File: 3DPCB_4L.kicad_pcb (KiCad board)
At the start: 4 copper layers, 100 x 60 mm, 757 parts, among them IC1 DRV8825, IC2 DRV8825, IC3 DRV8825, IC4 DRV8825, IC5 DRV8825, IC6 MP9943, J10 , J11 , J12 , J13 , J14 , J15 , J16 , J2 , J3 , J4 , J5 , J6 , J7 , J8 , J9 , K1 CONN_3, K2 CONN_3, K3 CONN_3, K4 CONN_3, K5 CONN_3, K6 CONN_3, K7 CONN_3, K8 CONN_3, K9 CONN_3, P1 CONN_8, P11 CONN_3X2, P12 CONN_3X2, P13 CONN_4, P2 CONN_8, P5 CONN_4, P6 CONN_4, P7 CONN_4, P8 CONN_2, P9 CONN_4, U1 CONN_4_LERCHE, U10 MICRO-SD, U11 TC4427, U12 MCP4728, U13 CONN_4_LERCHE, U15 SPST_MOMENTARY, U16 CONN_4_LERCHE, U2 SPST_MOMENTARY, U21 CONN_4_LERCHE, U22 CONN_4_LERCHE, U23 MCP4728, U24 IRFH5302, U25 CONN_4_LERCHE, U3 BSS84, U4 CONN_4_LERCHE, U5 IRFH5302, U6 LPC1768_TQFP100, U7 IRFH5302, U8 IRFH5302, U9 TC4427

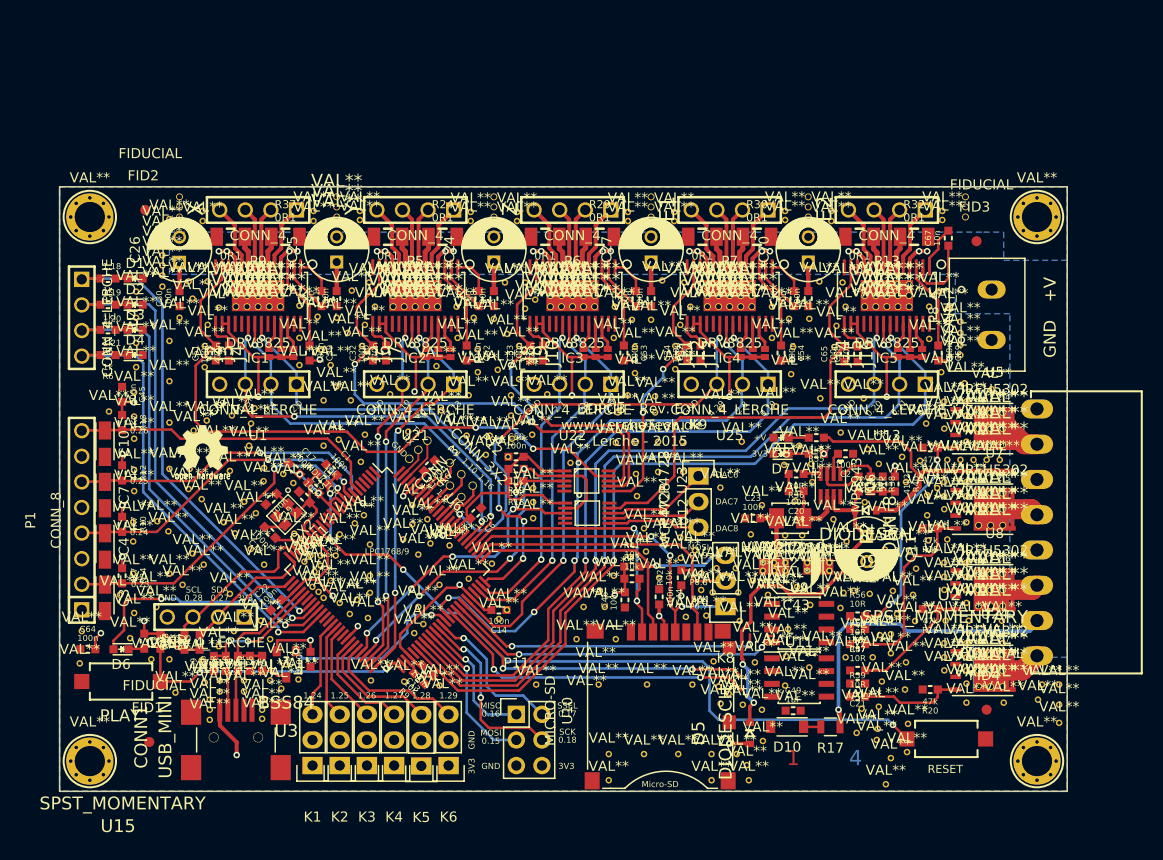
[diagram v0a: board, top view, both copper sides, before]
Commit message: Updated PCB
Updated PCB, splitting power for MOSFETs and motor-drivers.
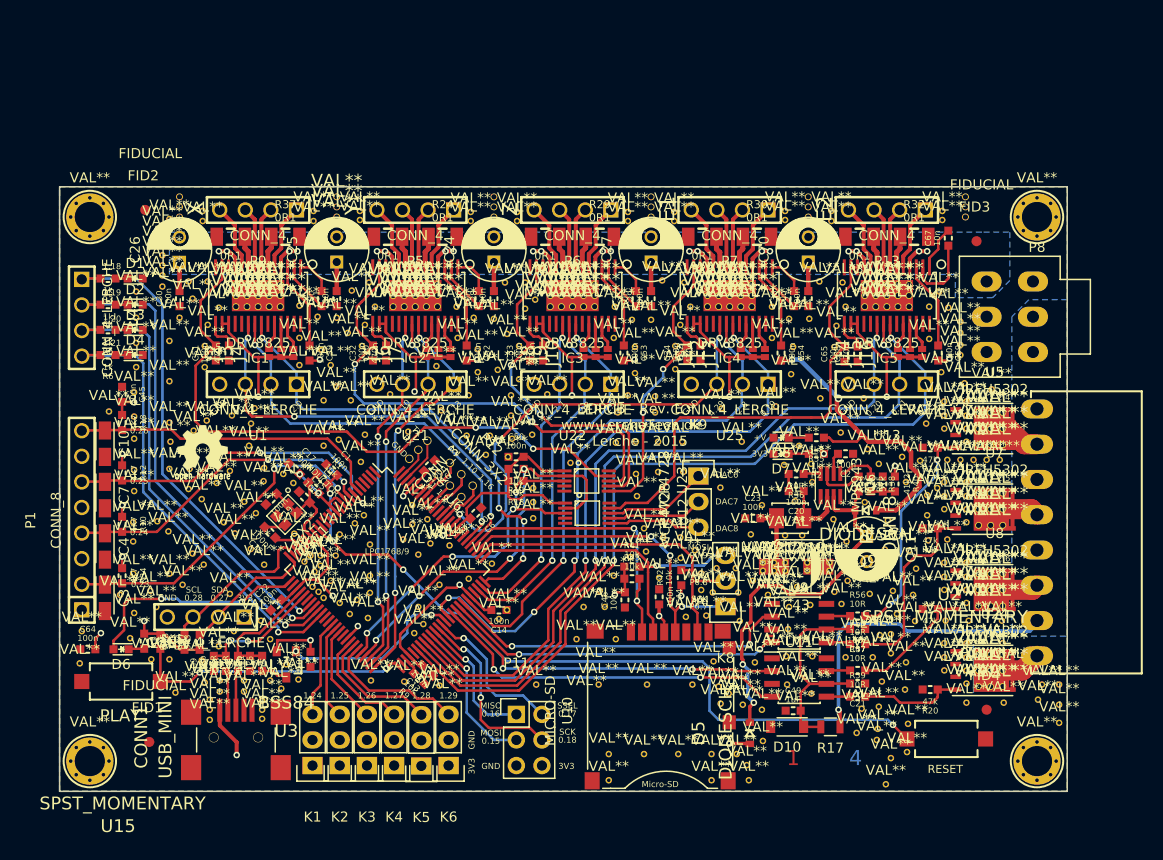
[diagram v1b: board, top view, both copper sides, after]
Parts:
- added ?: VAL**, Lerche_via_0.35_GND, F.Cu at (145.6, 164.9)
- added ?: VAL**, Lerche_via_0.35_GND, F.Cu at (141.0, 160.8)
- added ?: VAL**, Lerche_via_0.35_GND, F.Cu at (202.4, 177.2)
- added ?: VAL**, Lerche_via_0.35_GND, F.Cu at (204.6, 185.8)
- P8: value CONN_2 -> CONN_02X03; footprint LercheTech:Lerche_2P_5MM -> LercheTech:Lerche_2x3P_3.5mm_Molex_UltraFit
- moved P8 1.81 mm to (224.3, 148.4), turned to 270 degrees
- moved ? 1.17 mm to (208.2, 174.6)
- moved ? 1.14 mm to (204.7, 182.1)
- moved ? 0.91 mm to (206.9, 175.7)
- moved ? 0.41 mm to (207.6, 176.9)
- moved ? 0.22 mm to (202.2, 184.9)
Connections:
- CONN1 pad 4: (no net) -> Net-(CONN1-Pad4)
- IC1 pad 18: (no net) -> ~FAULT1
- IC1 pad 19: (no net) -> Net-(IC1-Pad19)
- IC1 pad 27: (no net) -> ~HOME1
- IC2 pad 18: (no net) -> ~FAULT2
- IC2 pad 19: (no net) -> Net-(IC2-Pad19)
- IC2 pad 27: (no net) -> ~HOME2
- IC3 pad 18: (no net) -> ~FAULT3
- IC3 pad 19: (no net) -> Net-(IC3-Pad19)
- IC3 pad 27: (no net) -> ~HOME3
- IC4 pad 18: (no net) -> ~FAULT4
- IC4 pad 19: (no net) -> Net-(IC4-Pad19)
- IC4 pad 27: (no net) -> ~HOME4
- IC5 pad 18: (no net) -> ~FAULT5
- IC5 pad 19: (no net) -> Net-(IC5-Pad19)
- IC5 pad 27: (no net) -> ~HOME5
- IC6 pad 8: (no net) -> Net-(IC6-Pad8)
- P2 pad 2: +12V -> V_MOSFET
- P2 pad 4: +12V -> V_MOSFET
- P2 pad 6: +12V -> V_MOSFET
- P2 pad 8: +12V -> V_MOSFET
- R17 pad 1: +12V -> V_MOSFET
- U10 pad 9: (no net) -> Net-(U10-Pad9)
- U12 pad 5: (no net) -> Net-(U12-Pad5)
- U23 pad 5: (no net) -> Net-(U23-Pad5)
- U6 pad 1: (no net) -> Net-(U6-Pad1)
- U6 pad 100: (no net) -> Net-(U6-Pad100)
- U6 pad 13: (no net) -> Net-(U6-Pad13)
- U6 pad 14: (no net) -> Net-(U6-Pad14)
- U6 pad 16: (no net) -> Net-(U6-Pad16)
- U6 pad 18: (no net) -> Net-(U6-Pad18)
- U6 pad 2: (no net) -> Net-(U6-Pad2)
- U6 pad 20: (no net) -> P1.31
- U6 pad 21: (no net) -> P1.30
- U6 pad 23: (no net) -> Net-(U6-Pad23)
- U6 pad 27: (no net) -> SD_IRQ
- U6 pad 3: (no net) -> Net-(U6-Pad3)
- U6 pad 36: (no net) -> P1.22
- U6 pad 37: (no net) -> P1.23
- U6 pad 4: (no net) -> Net-(U6-Pad4)
- U6 pad 5: (no net) -> Net-(U6-Pad5)
- U6 pad 52: (no net) -> SD_CD
- U6 pad 82: (no net) -> Net-(U6-Pad82)
- U6 pad 86: (no net) -> Net-(U6-Pad86)
- U6 pad 89: (no net) -> Net-(U6-Pad89)
- U6 pad 92: (no net) -> Net-(U6-Pad92)
- U6 pad 95: (no net) -> Net-(U6-Pad95)
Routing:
- net V_MOSFET: track 0.00 -> 30.4 mm, vias 0 -> 1
- net +12V: track 106.9 -> 78.2 mm, vias 27 -> 26
- net MOSVCC: track 2.15 -> 21.3 mm
- net P2.7: track 32.6 -> 35.9 mm
- net P2.4: track 31.3 -> 34.4 mm
- net P2.6: track 31.7 -> 34.5 mm
- net Net-(R56-Pad1): track 0.09 -> 2.47 mm
- net Net-(R57-Pad1): track 0.18 -> 2.56 mm
- net Net-(R59-Pad1): track 0.01 -> 2.37 mm
- net Net-(R58-Pad1): track 0.28 -> 2.43 mm
- net P2.5: track 32.2 -> 33.4 mm
- added copper zone on B.Cu, net V_MOSFET
- added copper zone on Inner2.Cu, net V_MOSFET
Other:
- board text added: "VMOS"
- board text added: "VMOT"
- board text removed: "Three Dimensional Printer Controller Board (3DPCB) - Rev. E Smoothie-compatible - www.smoothieware.org"

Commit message: Minor changes DONT USE NOW
Do not use this right now, changes are still coming in.
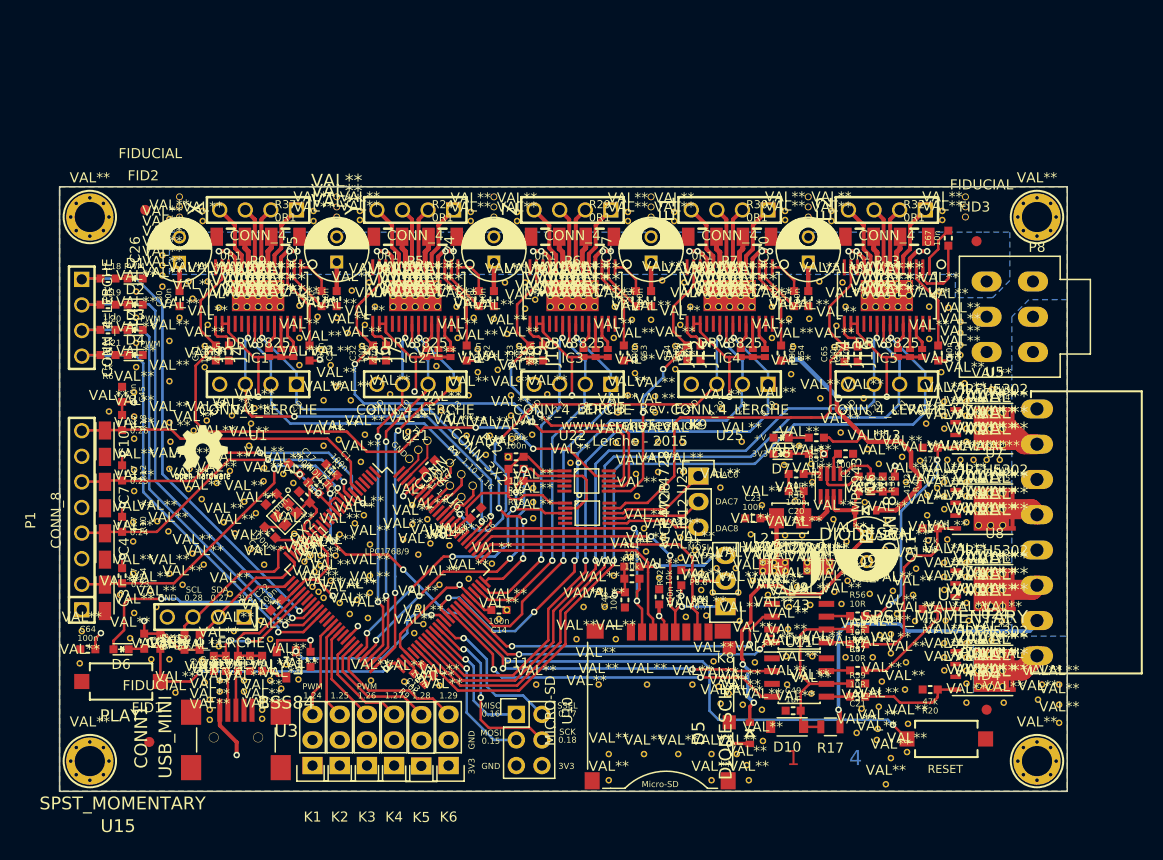
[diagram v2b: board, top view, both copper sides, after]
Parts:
- L2: value IHLP1212-10uH -> IHLP1212-2.2uH
- moved ? 1.14 mm to (222.5, 180.5)
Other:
- board text added: "PWM"
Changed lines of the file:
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@@
 (kicad_pcb (version 4) (host pcbnew 4.0.2-stable)
   (general
-    (links 1061)
+    (links 0)
     (no_connects 0)
-    (area 129.924999 135.424999 230.075001 195.575001)
+    (area 125.893917 130.7236 237.651491 200.3226)
     (thickness 1.6)
-    (drawings 128)
+    (drawings 135)
     (tracks 1506)
     (zones 0)
@@
   )
   (setup
-    (last_trace_width 0.254)
+    (last_trace_width 0.1524)
     (user_trace_width 0.2)
     (user_trace_width 0.254)
@@
     (mod_text_size 1 1)
     (mod_text_width 0.15)
-    (pad_size 1.58 2.35)
-    (pad_drill 0)
+    (pad_size 2 3)
+    (pad_drill 1.2)
     (pad_to_mask_clearance 0)
     (aux_axis_origin 130 195.5)
@@
   )
   (module Lerche_via_0.35mm_GND_MaskOver (layer F.Cu)
-    (at 223.6 180.8)
+    (at 222.5 180.5)
     (attr smd)
     (fp_text reference "" (at 0 -2.9) (layer F.SilkS)
@@
   (module LercheTech:Lerche_IHLP-1212BZ-11_Inductor (layer F.Cu)
     (at 202.5 168.4 180)
-    (fp_text reference L2 (at 0 -4.4 180) (layer F.SilkS)
+    (fp_text reference L2 (at 2.9 -2 180) (layer F.SilkS)
       (effects (font (size 1 1) (thickness 0.15)))
     )
-    (fp_text value IHLP1212-10uH (at 0 -2.9 180) (layer F.SilkS)
+    (fp_text value IHLP1212-2.2uH (at 0 -2.9 180) (layer F.SilkS)
       (effects (font (size 1 1) (thickness 0.15)))
     )
@@
     (fp_line (start -6 5) (end 6 5) (layer F.SilkS) (width 0.15))
     (pad 1 thru_hole oval (at -3.5 -2.3 270) (size 2 3) (drill 1.2) (layers *.Cu *.Mask F.SilkS)
-      (net 19 GND))
+      (net 19 GND) (zone_connect 2))
     (pad 2 thru_hole oval (at -3.5 2.3 270) (size 2 3) (drill 1.2) (layers *.Cu *.Mask F.SilkS)
       (net 1 +12V))
@@
       (net 189 V_MOSFET))
     (pad 4 thru_hole oval (at 0 2.3 270) (size 2 3) (drill 1.2) (layers *.Cu *.Mask F.SilkS)
-      (net 19 GND))
+      (net 19 GND) (zone_connect 2))
     (pad 5 thru_hole oval (at 3.5 -2.3 270) (size 2 3) (drill 1.2) (layers *.Cu *.Mask F.SilkS)
       (net 189 V_MOSFET))
     (pad 6 thru_hole oval (at 3.5 2.3 270) (size 2 3) (drill 1.2) (layers *.Cu *.Mask F.SilkS)
-      (net 19 GND))
+      (net 19 GND) (zone_connect 2))
+  )
+  (gr_text PWM (at 139 151.1) (layer F.SilkS)
+    (effects (font (size 0.6 0.6) (thickness 0.1)))
+  )
+  (gr_text PWM (at 139 148.6) (layer F.SilkS)
+    (effects (font (size 0.6 0.6) (thickness 0.1)))
+  )
+  (gr_text PWM (at 137.4 143.4) (layer F.SilkS)
+    (effects (font (size 0.6 0.6) (thickness 0.1)))
+  )
+  (gr_text PWM (at 223.7 155.6) (layer F.SilkS)
+    (effects (font (size 0.6 0.6) (thickness 0.1)))
+  )
+  (gr_text PWM (at 223.7 163.6) (layer F.SilkS)
+    (effects (font (size 0.6 0.6) (thickness 0.1)))
+  )
+  (gr_text PWM (at 155.1 185.1) (layer F.SilkS)
+    (effects (font (size 0.6 0.6) (thickness 0.1)))
+  )
+  (gr_text PWM (at 160.5 185.1) (layer F.SilkS)
+    (effects (font (size 0.6 0.6) (thickness 0.1)))
   )
   (gr_text VMOS (at 229 152.4 270) (layer B.SilkS)

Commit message: First A5984 in place - DO NOT USE
First A5984 in place - DO NOT USE
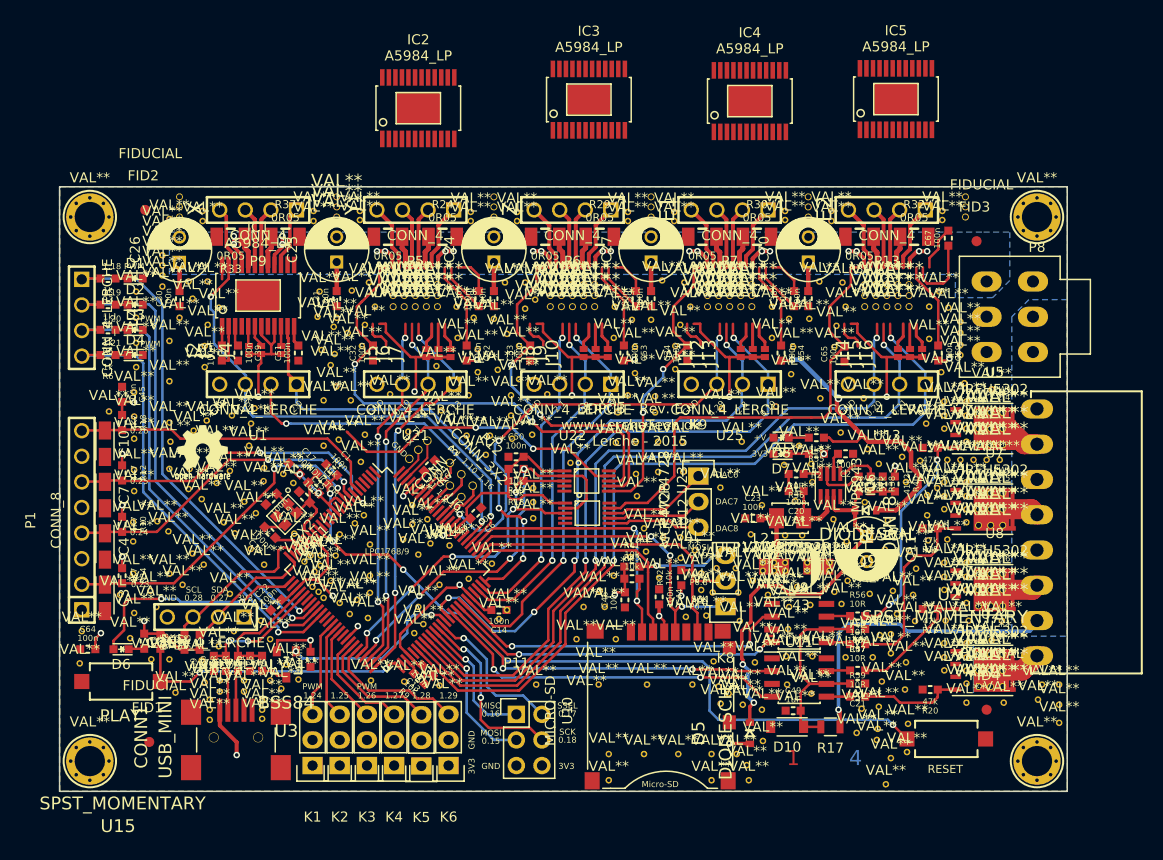
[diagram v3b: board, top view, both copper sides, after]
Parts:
- removed the ? at (174.5, 162.3)
- removed the ? at (147.5, 145.2)
- removed the ? at (151.9, 145.2)
- removed the ? at (147.5, 147.4)
- removed the ? at (151.9, 147.4)
- removed the ? at (147.5, 146.3)
- removed the ? at (151.9, 146.3)
- removed the ? at (149.7, 145.2)
- removed the ? at (149.7, 146.3)
- removed the ? at (149.7, 147.4)
- removed the ? at (148.6, 145.2)
- removed the ? at (148.6, 146.3)
- removed the ? at (148.6, 147.4)
- removed the ? at (150.8, 147.4)
- removed the ? at (150.8, 146.3)
- removed the ? at (150.8, 145.2)
- removed C35, C40, C41, C42, C68: 470n, LercheTech:Lerche_C0603
- C36, C37, C8: value 10n -> 100nF
- C67: value 10n -> 100n
- IC1, IC2, IC3, IC4, IC5: value DRV8825 -> A5984_LP; footprint LercheTech:Lerche_TSSOP28_EP -> LercheTech:Lerche_TSSOP24_EP
- L2: value IHLP1212-2.2uH -> IHLP1212BZER2R2M11
- R21, R22, R23, R24, R29, R30, R31, R32, R33, R37: value 0R1 -> 0R05
- moved IC5 19.5 mm to (213.0, 126.8), turned to 0 degrees
- moved IC3 19.5 mm to (182.5, 126.8), turned to 0 degrees
- moved IC4 19.4 mm to (198.5, 127.0), turned to 0 degrees
- moved IC2 18.6 mm to (165.6, 127.7), turned to 0 degrees
- moved C8 11.3 mm to (146.1, 152.0)
- moved C51 8.20 mm to (153.7, 152.0)
- moved C39 7.10 mm to (147.7, 152.0)
- moved ? 3.67 mm to (157.3, 152.1)
- moved ? 3.57 mm to (157.2, 149.4)
- moved ? 2.44 mm to (155.8, 145.9)
- moved J2 2.02 mm to (148.8, 151.7)
- moved J3 2.02 mm to (150.0, 151.7)
- moved J4 1.24 mm to (152.0, 151.7)
- turned IC1 to 0 degrees
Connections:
- net SD_CD renamed P2.11
- IC1 pad 11: +12V -> STP1
- IC1 pad 13: VREF1 -> GND
- IC1 pad 14: GND -> DIR1
- IC1 pad 15: Net-(C35-Pad1) -> Net-(IC1-Pad15)
- IC1 pad 16: +3.3V -> +12V
- IC1 pad 17: +3.3V -> Net-(IC1-Pad17)
- IC1 pad 18: ~FAULT1 -> Net-(IC1-Pad18)
- IC1 pad 20: DIR1 -> Net-(IC1-Pad20)
- IC1 pad 21: EN1 -> +12V
- IC1 pad 22: STP1 -> Net-(IC1-Pad22)
- IC1 pad 23: (no net) -> EN1
- IC1 pad 24: Net-(IC1-Pad24) -> GND
- IC1 pad 25: Net-(IC1-Pad25) -> GND
- IC1 pad 4: +12V -> Net-(IC1-Pad4)
- IC1 pad 7: Net-(IC1-Pad7) -> +3.3V
- IC1 pad 8: Net-(IC1-Pad8) -> GND
- IC1 pad 9: Net-(IC1-Pad9) -> +3.3V
- IC2 pad 11: +12V -> STP2
- IC2 pad 13: VREF2 -> GND
- IC2 pad 14: GND -> DIR2
- IC2 pad 15: Net-(C40-Pad1) -> Net-(IC2-Pad15)
- IC2 pad 16: +3.3V -> +12V
- IC2 pad 17: +3.3V -> Net-(IC2-Pad17)
- IC2 pad 18: ~FAULT2 -> Net-(IC2-Pad18)
- IC2 pad 20: DIR2 -> Net-(IC2-Pad20)
- IC2 pad 21: EN2 -> +12V
- IC2 pad 22: STP2 -> Net-(IC2-Pad22)
- IC2 pad 23: (no net) -> EN2
- IC2 pad 24: Net-(IC2-Pad24) -> GND
- IC2 pad 25: Net-(IC2-Pad25) -> GND
- IC2 pad 4: +12V -> Net-(IC2-Pad4)
- IC2 pad 7: Net-(IC2-Pad7) -> +3.3V
- IC2 pad 8: Net-(IC2-Pad8) -> GND
- IC2 pad 9: Net-(IC2-Pad9) -> +3.3V
- IC3 pad 11: +12V -> STP3
- IC3 pad 13: VREF3 -> GND
- IC3 pad 14: GND -> DIR3
- IC3 pad 15: Net-(C41-Pad1) -> Net-(IC3-Pad15)
- IC3 pad 16: +3.3V -> +12V
- IC3 pad 17: +3.3V -> Net-(IC3-Pad17)
- IC3 pad 18: ~FAULT3 -> Net-(IC3-Pad18)
- IC3 pad 20: DIR3 -> Net-(IC3-Pad20)
- IC3 pad 21: EN3 -> +12V
- IC3 pad 22: STP3 -> Net-(IC3-Pad22)
- IC3 pad 23: (no net) -> EN3
- IC3 pad 24: Net-(IC3-Pad24) -> GND
- IC3 pad 25: Net-(IC3-Pad25) -> GND
- IC3 pad 4: +12V -> Net-(IC3-Pad4)
- IC3 pad 7: Net-(IC3-Pad7) -> +3.3V
- IC3 pad 8: Net-(IC3-Pad8) -> GND
- IC3 pad 9: Net-(IC3-Pad9) -> +3.3V
- IC4 pad 11: +12V -> STP4
- IC4 pad 13: VREF4 -> GND
- IC4 pad 14: GND -> DIR4
- IC4 pad 15: Net-(C42-Pad1) -> Net-(IC4-Pad15)
- IC4 pad 16: +3.3V -> +12V
- IC4 pad 17: +3.3V -> Net-(IC4-Pad17)
- IC4 pad 18: ~FAULT4 -> Net-(IC4-Pad18)
- IC4 pad 20: DIR4 -> Net-(IC4-Pad20)
- IC4 pad 21: EN4 -> +12V
- IC4 pad 22: STP4 -> Net-(IC4-Pad22)
- IC4 pad 23: (no net) -> EN4
- IC4 pad 24: Net-(IC4-Pad24) -> GND
- IC4 pad 25: Net-(IC4-Pad25) -> GND
- IC4 pad 4: +12V -> Net-(IC4-Pad4)
- IC4 pad 7: Net-(IC4-Pad7) -> +3.3V
- IC4 pad 8: Net-(IC4-Pad8) -> GND
- IC4 pad 9: Net-(IC4-Pad9) -> +3.3V
- IC5 pad 11: +12V -> STP5
- IC5 pad 13: VREF5 -> GND
- IC5 pad 14: GND -> DIR5
- IC5 pad 15: Net-(C68-Pad1) -> Net-(IC5-Pad15)
- IC5 pad 16: +3.3V -> +12V
- IC5 pad 17: +3.3V -> Net-(IC5-Pad17)
- IC5 pad 18: ~FAULT5 -> Net-(IC5-Pad18)
- IC5 pad 20: DIR5 -> Net-(IC5-Pad20)
- IC5 pad 21: EN5 -> +12V
- IC5 pad 22: STP5 -> Net-(IC5-Pad22)
- IC5 pad 23: (no net) -> EN5
- IC5 pad 24: Net-(IC5-Pad24) -> GND
- IC5 pad 25: Net-(IC5-Pad25) -> GND
- IC5 pad 4: +12V -> Net-(IC5-Pad4)
- IC5 pad 7: Net-(IC5-Pad7) -> +3.3V
- IC5 pad 8: Net-(IC5-Pad8) -> GND
- IC5 pad 9: Net-(IC5-Pad9) -> +3.3V
- J10 pad 2: Net-(IC3-Pad26) -> Net-(IC3-Pad10)
- J11 pad 2: Net-(IC4-Pad24) -> Net-(IC4-Pad5)
- J12 pad 2: Net-(IC4-Pad25) -> Net-(IC4-Pad6)
- J13 pad 2: Net-(IC4-Pad26) -> Net-(IC4-Pad10)
- J14 pad 2: Net-(IC5-Pad24) -> Net-(IC5-Pad5)
- J15 pad 2: Net-(IC5-Pad25) -> Net-(IC5-Pad6)
- J16 pad 2: Net-(IC5-Pad26) -> Net-(IC5-Pad10)
- J2 pad 2: Net-(IC1-Pad24) -> Net-(IC1-Pad5)
- J3 pad 2: Net-(IC1-Pad25) -> Net-(IC1-Pad6)
- J4 pad 2: Net-(IC1-Pad26) -> Net-(IC1-Pad10)
- J5 pad 2: Net-(IC2-Pad24) -> Net-(IC2-Pad5)
- J6 pad 2: Net-(IC2-Pad25) -> Net-(IC2-Pad6)
- J7 pad 2: Net-(IC2-Pad26) -> Net-(IC2-Pad10)
- J8 pad 2: Net-(IC3-Pad24) -> Net-(IC3-Pad5)
- J9 pad 2: Net-(IC3-Pad25) -> Net-(IC3-Pad6)
- P13 pad 1: Net-(IC5-Pad5) -> Net-(IC5-Pad15)
- P13 pad 2: Net-(IC5-Pad7) -> Net-(IC5-Pad18)
- P13 pad 3: Net-(IC5-Pad8) -> Net-(IC5-Pad19)
- P13 pad 4: Net-(IC5-Pad10) -> Net-(IC5-Pad22)
- P5 pad 1: Net-(IC2-Pad5) -> Net-(IC2-Pad15)
- P5 pad 2: Net-(IC2-Pad7) -> Net-(IC2-Pad18)
- P5 pad 3: Net-(IC2-Pad8) -> Net-(IC2-Pad19)
- P5 pad 4: Net-(IC2-Pad10) -> Net-(IC2-Pad22)
- P6 pad 1: Net-(IC3-Pad5) -> Net-(IC3-Pad15)
- P6 pad 2: Net-(IC3-Pad7) -> Net-(IC3-Pad18)
- P6 pad 3: Net-(IC3-Pad8) -> Net-(IC3-Pad19)
- P6 pad 4: Net-(IC3-Pad10) -> Net-(IC3-Pad22)
- P7 pad 1: Net-(IC4-Pad5) -> Net-(IC4-Pad15)
- P7 pad 2: Net-(IC4-Pad7) -> Net-(IC4-Pad18)
- P7 pad 3: Net-(IC4-Pad8) -> Net-(IC4-Pad19)
- P7 pad 4: Net-(IC4-Pad10) -> Net-(IC4-Pad22)
- P9 pad 1: Net-(IC1-Pad5) -> Net-(IC1-Pad15)
- P9 pad 2: Net-(IC1-Pad7) -> Net-(IC1-Pad18)
- P9 pad 3: Net-(IC1-Pad8) -> Net-(IC1-Pad19)
- P9 pad 4: Net-(IC1-Pad10) -> Net-(IC1-Pad22)
- R21 pad 1: Net-(IC2-Pad9) -> Net-(IC2-Pad20)
- R22 pad 1: Net-(IC3-Pad9) -> Net-(IC3-Pad20)
- R23 pad 1: Net-(IC4-Pad9) -> Net-(IC4-Pad20)
- R24 pad 1: Net-(IC2-Pad6) -> Net-(IC2-Pad17)
- R29 pad 1: Net-(IC3-Pad6) -> Net-(IC3-Pad17)
- R30 pad 1: Net-(IC4-Pad6) -> Net-(IC4-Pad17)
- R31 pad 1: Net-(IC5-Pad9) -> Net-(IC5-Pad20)
- R32 pad 1: Net-(IC5-Pad6) -> Net-(IC5-Pad17)
- R33 pad 1: Net-(IC1-Pad9) -> Net-(IC1-Pad20)
- R37 pad 1: Net-(IC1-Pad6) -> Net-(IC1-Pad17)
- U1 pad 2: EN1 -> DIR1
- U1 pad 3: DIR1 -> EN1
- U13 pad 2: EN5 -> DIR5
- U13 pad 3: DIR5 -> EN5
- U21 pad 2: EN2 -> DIR2
- U21 pad 3: DIR2 -> EN2
- U22 pad 2: EN3 -> DIR3
- U22 pad 3: DIR3 -> EN3
- U25 pad 2: EN4 -> DIR4
- U25 pad 3: DIR4 -> EN4
- U6 pad 48: DIR2 -> EN2
- U6 pad 49: EN2 -> DIR2
- U6 pad 57: EN5 -> DIR5
- U6 pad 58: DIR5 -> EN5
- U6 pad 65: EN4 -> DIR4
- U6 pad 73: EN3 -> DIR3
- U6 pad 74: DIR3 -> EN3
- U6 pad 80: DIR1 -> EN1
- U6 pad 81: EN1 -> DIR1
- U6 pad 85: DIR4 -> EN4
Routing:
- net (no net): track 0.68 -> 35.6 mm, vias 0 -> 16
- net VREF1: track 63.5 -> 31.9 mm
- net +12V: track 78.2 -> 55.1 mm, vias 26 -> 9
- net EN4: track 57.8 -> 45.4 mm, vias 4 -> 3
- net DIR4: track 45.4 -> 57.8 mm, vias 3 -> 4
- net EN1: track 39.1 -> 51.0 mm
- net DIR1: track 43.0 -> 33.0 mm, vias 3 -> 2
- net Net-(C39-Pad2): track 8.65 -> 2.01 mm
- net Net-(IC5-Pad22): track 0.00 -> 6.61 mm
- net Net-(IC5-Pad15): track 0.00 -> 6.61 mm
- net Net-(IC4-Pad22): track 0.00 -> 6.61 mm
- net Net-(IC4-Pad15): track 0.00 -> 6.61 mm
- net Net-(IC3-Pad22): track 0.00 -> 6.61 mm
- net Net-(IC3-Pad15): track 0.00 -> 6.61 mm
- net Net-(IC2-Pad22): track 0.00 -> 6.61 mm
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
